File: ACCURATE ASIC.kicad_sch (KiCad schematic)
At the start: 51 parts, among them IC1 CERN_aCCURATE2_A_Chip1, IC2 AD817ARZ, IC3 DAC7578SRGE, IC4 AD817ARZ, IC5 AD817ARZ, IC6 ADR443BRZ, IC7 NL17SV16XV5T2G, U1 SHT4x

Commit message: Begun schematics
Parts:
- removed C11, C26, C28: CC0603_100NF_50V_10%_X7R, Capacitors SMD:CAPC1608X87N, symbol Capacitors SMD:CC0603_100NF_50V_10%_X7R
- removed C27: CC0603_10UF_25V_20%_X5R, Capacitors SMD:CAPC1709X100N, symbol Capacitors SMD:CC0603_10UF_25V_20%_X5R
- removed IC6: ADR443BRZ, ICs And Semiconductors SMD:SOIC127P600X175-8N, symbol Regulators:ADR443BRZ
- removed IC7: NL17SV16XV5T2G, ICs And Semiconductors SMD:SOTFL50P160X60-5N, symbol Standard Logic:NL17SV16XV5T2G
- removed R14, R15: R0603_0R_JUMPER, Resistors SMD:RESC1608X55N, symbol Resistors SMD:R0603_0R_JUMPER
- removed R2, R3: R0805_10K_0.1%_0.1W_10PPM, Resistors SMD:RESC2012X60N, symbol Resistors SMD:R0805_10K_0.1%_0.1W_10PPM
- removed U1: SHT4x, Sensor_Humidity:Sensirion_DFN-4_1.5x1.5mm_P0.8mm_SHT4x_NoCentralPad, symbol Sensor_Humidity:SHT4x
- added C67, C69: CC0603_100NF_50V_10%_X7R, Capacitors SMD:CAPC1608X87N, symbol Capacitors SMD:CC0603_100NF_50V_10%_X7R
- added C68: CC0603_220NF_10V_10%_X7R, Capacitors SMD:CAPC1608X87N, symbol Capacitors SMD:CC0603_220NF_10V_10%_X7R
- added C70: CC0603_10UF_25V_20%_X5R, Capacitors SMD:CAPC1709X100N, symbol Capacitors SMD:CC0603_10UF_25V_20%_X5R
- added J8: Conn_02x04_Counter_Clockwise, symbol Connector_Generic:Conn_02x04_Counter_Clockwise
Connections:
- net GND: now also C69.2, C70.2
- net SCL: now also J8.5 (Pin_5), J8.7 (Pin_7)
- net SDA: now also J8.6 (Pin_6), J8.8 (Pin_8)
- net Vcm_Buf: now also C67.1, C68.1, C69.1, C70.1
- net at IC1.2, TP1.1: now also C67.2, C68.2
- net +5VA renamed +5V
- net 3V3_Ref renamed 3V_Ref
- new net FPGA_SCL: J8.2 (Pin_2)
- new net FPGA_SDA: J8.1 (Pin_1)
- new net MCU_SCL: J8.4 (Pin_4)
- new net MCU_SDA: J8.3 (Pin_3)
- no-connect marks 20 -> 17
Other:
- note added: ": :||"
- note added: "||: :"
- note removed: "3V3 Reference"
- note removed: "ACCURATE2 Clock Generation"
- note removed: "Humidity and Temperature sensor"
- moved on the sheet: C1, C2, C3, C4, C5, C6, C7, C8, IC1, R1, TP1

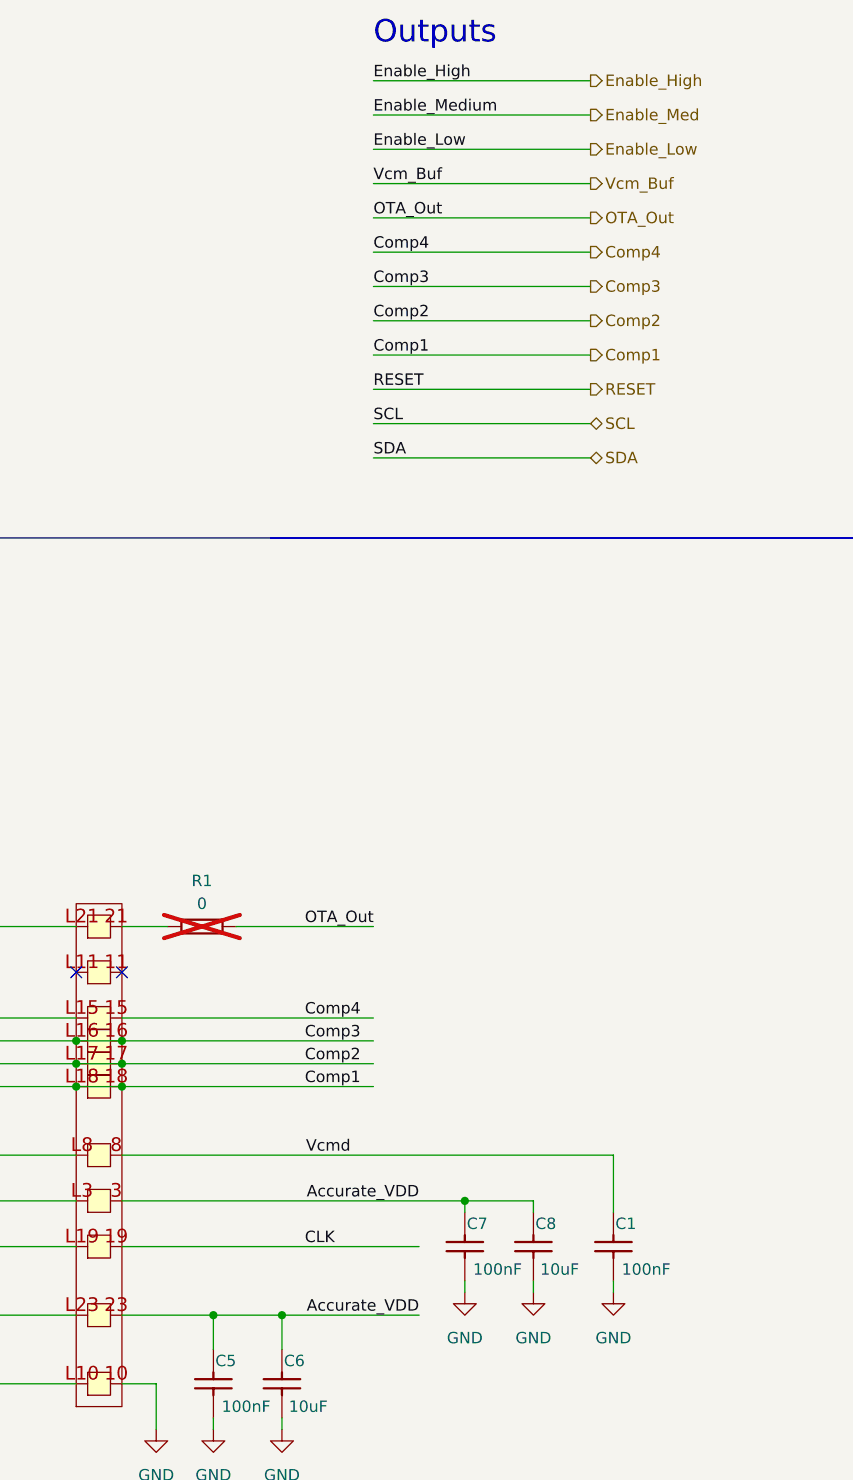
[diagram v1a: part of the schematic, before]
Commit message: Connected FPGA to Accurate, added Atsam, fixed some Accurate connections
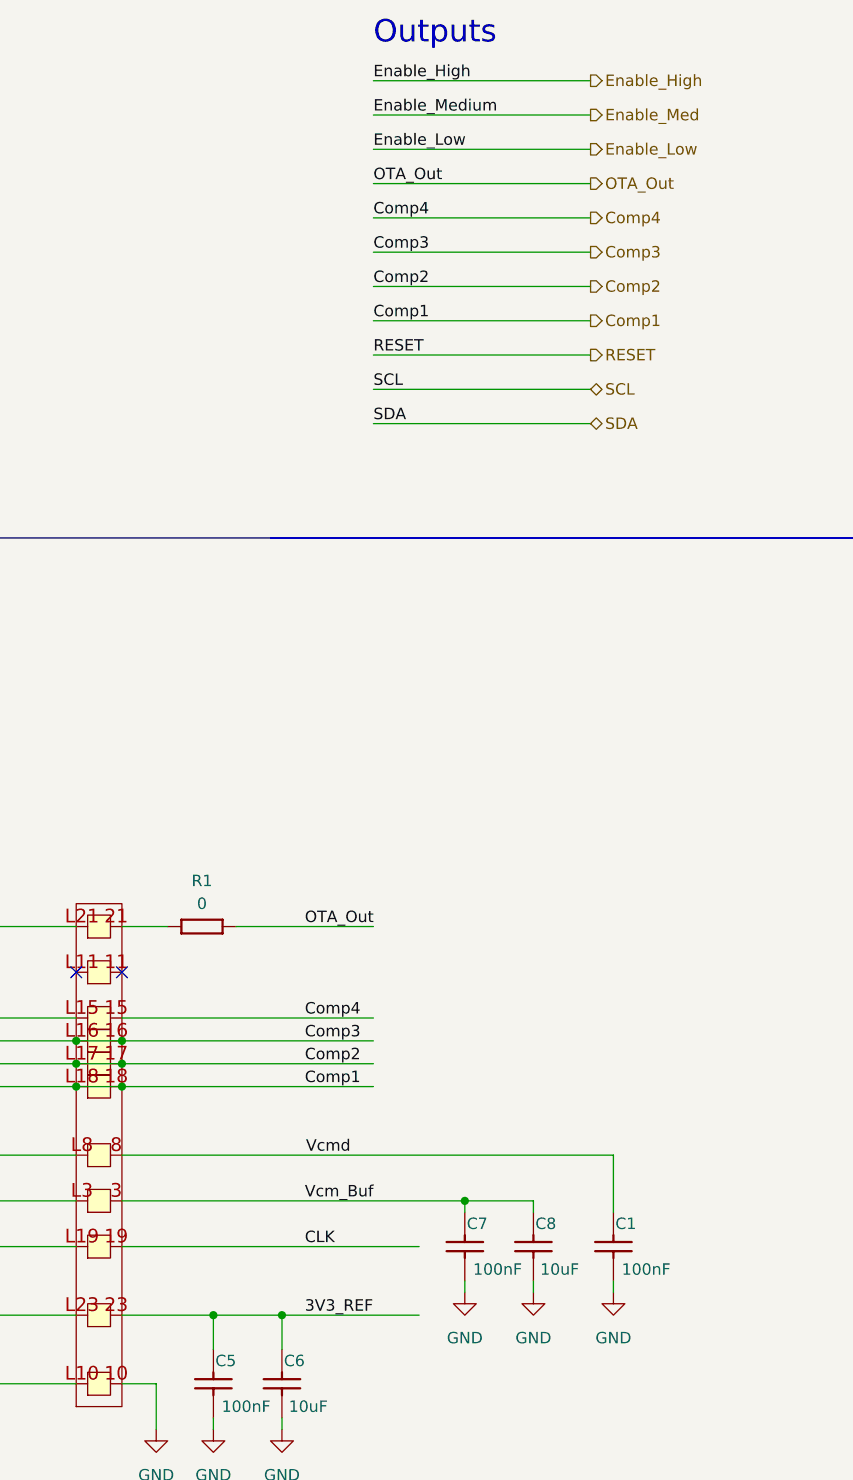
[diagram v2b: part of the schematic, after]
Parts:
- R1: now fitted
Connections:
- net 3V3_REF: now also C5.1, C6.1, IC1.23
- net Vcm_Buf: now also C7.1, C8.1, IC1.3
- removed net Accurate_VDD: C5.1, C6.1, C7.1, C8.1, IC1.23, IC1.3
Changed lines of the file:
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@@
     (stroke (width 0) (type default))
   )
-  (wire (pts (xy 339.09 43.18) (xy 363.22 43.18))
+  (wire (pts (xy 339.09 39.37) (xy 363.22 39.37))
     (stroke (width 0) (type default))
   )
@@
     (stroke (width 0) (type default))
   )
-  (wire (pts (xy 339.09 35.56) (xy 363.22 35.56))
-    (stroke (width 0) (type default))
-  )
   (wire (pts (xy 228.6 101.6) (xy 232.41 101.6))
     (stroke (width 0) (type default))
@@
     (stroke (width 0) (type default))
   )
-  (wire (pts (xy 311.15 148.59) (xy 349.25 148.59))
-    (stroke (width 0) (type default))
-  )
   (polyline (pts (xy 327.66 74.93) (xy 407.9748 74.93))
     (stroke (width 0) (type default))
@@
     (stroke (width 0) (type default))
   )
-  (wire (pts (xy 339.09 39.37) (xy 363.22 39.37))
+  (wire (pts (xy 339.09 35.56) (xy 363.22 35.56))
     (stroke (width 0) (type default))
   )
@@
     (stroke (width 0) (type default))
   )
-  (wire (pts (xy 339.09 58.42) (xy 363.22 58.42))
+  (wire (pts (xy 339.09 54.61) (xy 363.22 54.61))
     (stroke (width 0) (type default))
   )
@@
     (stroke (width 0) (type default))
   )
+  (wire (pts (xy 311.15 148.59) (xy 349.25 148.59))
+    (stroke (width 0) (type default))
+  )
   (wire (pts (xy 55.88 222.25) (xy 58.42 222.25))
     (stroke (width 0) (type default))
@@
     (stroke (width 0) (type default))
   )
-  (wire (pts (xy 339.09 54.61) (xy 363.22 54.61))
+  (wire (pts (xy 339.09 50.8) (xy 363.22 50.8))
     (stroke (width 0) (type default))
   )
@@
     (stroke (width 0) (type default))
   )
-  (wire (pts (xy 339.09 46.99) (xy 363.22 46.99))
+  (wire (pts (xy 339.09 43.18) (xy 363.22 43.18))
     (stroke (width 0) (type default))
   )
-  (wire (pts (xy 339.09 50.8) (xy 363.22 50.8))
+  (wire (pts (xy 339.09 46.99) (xy 363.22 46.99))
     (stroke (width 0) (type default))
   )
@@
     (stroke (width 0) (type default))
   )
-  (wire (pts (xy 339.09 62.23) (xy 363.22 62.23))
+  (wire (pts (xy 339.09 58.42) (xy 363.22 58.42))
     (stroke (width 0) (type default))
   )
@@
     (stroke (width 0) (type default))
   )
-  (wire (pts (xy 339.09 66.04) (xy 363.22 66.04))
+  (wire (pts (xy 339.09 62.23) (xy 363.22 62.23))
     (stroke (width 0) (type default))
   )
@@
     (effects (font (size 1.27 1.27)) (justify left bottom))
   )
-  (label "Comp3" (at 339.09 46.99 0) (fields_autoplaced)
+  (label "Comp3" (at 339.09 43.18 0) (fields_autoplaced)
     (effects (font (size 1.27 1.27)) (justify left bottom))
   )
@@
     (effects (font (size 1.27 1.27)) (justify right bottom))
   )
-  (label "Comp2" (at 339.09 50.8 0) (fields_autoplaced)
+  (label "Comp2" (at 339.09 46.99 0) (fields_autoplaced)
     (effects (font (size 1.27 1.27)) (justify left bottom))
   )
@@
     (effects (font (size 1.27 1.27)) (justify left bottom))
   )
-  (label "Comp1" (at 339.09 54.61 0) (fields_autoplaced)
+  (label "Comp1" (at 339.09 50.8 0) (fields_autoplaced)
     (effects (font (size 1.27 1.27)) (justify left bottom))
   )
@@
     (effects (font (size 1.27 1.27)) (justify left bottom))
   )
-  (label "Comp4" (at 339.09 43.18 0) (fields_autoplaced)
+  (label "Comp4" (at 339.09 39.37 0) (fields_autoplaced)
     (effects (font (size 1.27 1.27)) (justify left bottom))
   )
-  (label "Accurate_VDD" (at 344.17 161.29 180) (fields_autoplaced)
-    (effects (font (size 1.27 1.27)) (justify right bottom))
+  (label "Vcm_Buf" (at 331.47 148.59 0) (fields_autoplaced)
+    (effects (font (size 1.27 1.27)) (justify left bottom))
   )
   (label "3V_REF" (at 41.91 72.39 0) (fields_autoplaced)
@@
     (effects (font (size 1.27 1.27)) (justify left bottom))
   )
-  (label "SCL" (at 339.09 62.23 0) (fields_autoplaced)
+  (label "SCL" (at 339.09 58.42 0) (fields_autoplaced)
     (effects (font (size 1.27 1.27)) (justify left bottom))
   )
@@
     (effects (font (size 1.27 1.27)) (justify right bottom))
   )
+  (label "3V3_REF" (at 331.47 161.29 0) (fields_autoplaced)
+    (effects (font (size 1.27 1.27)) (justify left bottom))
+  )
   (label "Comp1" (at 331.47 135.89 0) (fields_autoplaced)
     (effects (font (size 1.27 1.27)) (justify left bottom))
@@
     (effects (font (size 1.27 1.27)) (justify left bottom))
   )
-  (label "SDA" (at 339.09 66.04 0) (fields_autoplaced)
+  (label "SDA" (at 339.09 62.23 0) (fields_autoplaced)
     (effects (font (size 1.27 1.27)) (justify left bottom))
   )
@@
     (effects (font (size 1.27 1.27)) (justify left bottom))
   )
-  (label "OTA_Out" (at 339.09 39.37 0) (fields_autoplaced)
+  (label "OTA_Out" (at 339.09 35.56 0) (fields_autoplaced)
     (effects (font (size 1.27 1.27)) (justify left bottom))
   )
@@
     (effects (font (size 1.27 1.27)) (justify left bottom))
   )
-  (label "Vcm_Buf" (at 339.09 35.56 0) (fields_autoplaced)
-    (effects (font (size 1.27 1.27)) (justify left bottom))
-  )
   (label "FPGA_SDA" (at 86.36 34.29 0) (fields_autoplaced)
     (effects (font (size 1.27 1.27)) (justify left bottom))
   )
-  (label "Accurate_VDD" (at 344.17 148.59 180) (fields_autoplaced)
-    (effects (font (size 1.27 1.27)) (justify right bottom))
-  )
   (label "Enable_Low" (at 226.06 156.21 0) (fields_autoplaced)
     (effects (font (size 1.27 1.27)) (justify left bottom))
   )
-  (label "RESET" (at 339.09 58.42 0) (fields_autoplaced)
+  (label "RESET" (at 339.09 54.61 0) (fields_autoplaced)
     (effects (font (size 1.27 1.27)) (justify left bottom))
   )
@@
     (effects (font (size 1.27 1.27)) (justify left bottom))
   )
-  (hierarchical_label "Comp2" (shape output) (at 363.22 50.8 0) (fields_autoplaced)
+  (hierarchical_label "Comp2" (shape output) (at 363.22 46.99 0) (fields_autoplaced)
     (effects (font (size 1.27 1.27)) (justify left))
   )
-  (hierarchical_label "SDA" (shape bidirectional) (at 363.22 66.04 0) (fields_autoplaced)
+  (hierarchical_label "SDA" (shape bidirectional) (at 363.22 62.23 0) (fields_autoplaced)
     (effects (font (size 1.27 1.27)) (justify left))
   )
-  (hierarchical_label "Comp1" (shape output) (at 363.22 54.61 0) (fields_autoplaced)
+  (hierarchical_label "Comp1" (shape output) (at 363.22 50.8 0) (fields_autoplaced)
     (effects (font (size 1.27 1.27)) (justify left))
   )
-  (hierarchical_label "RESET" (shape output) (at 363.22 58.42 0) (fields_autoplaced)
+  (hierarchical_label "RESET" (shape output) (at 363.22 54.61 0) (fields_autoplaced)
     (effects (font (size 1.27 1.27)) (justify left))
   )
@@
     (effects (font (size 1.27 1.27)) (justify left))
   )
-  (hierarchical_label "OTA_Out" (shape output) (at 363.22 39.37 0) (fields_autoplaced)
+  (hierarchical_label "OTA_Out" (shape output) (at 363.22 35.56 0) (fields_autoplaced)
     (effects (font (size 1.27 1.27)) (justify left))
   )
@@
     (effects (font (size 1.27 1.27)) (justify right))
   )
-  (hierarchical_label "Comp4" (shape output) (at 363.22 43.18 0) (fields_autoplaced)
+  (hierarchical_label "Comp4" (shape output) (at 363.22 39.37 0) (fields_autoplaced)
     (effects (font (size 1.27 1.27)) (justify left))
   )
@@
     (effects (font (size 1.27 1.27)) (justify right))
   )
-  (hierarchical_label "SCL" (shape bidirectional) (at 363.22 62.23 0) (fields_autoplaced)
+  (hierarchical_label "SCL" (shape bidirectional) (at 363.22 58.42 0) (fields_autoplaced)
     (effects (font (size 1.27 1.27)) (justify left))
   )
-  (hierarchical_label "Comp3" (shape output) (at 363.22 46.99 0) (fields_autoplaced)
-    (effects (font (size 1.27 1.27)) (justify left))
-  )
-  (hierarchical_label "Vcm_Buf" (shape output) (at 363.22 35.56 0) (fields_autoplaced)
+  (hierarchical_label "Comp3" (shape output) (at 363.22 43.18 0) (fields_autoplaced)
     (effects (font (size 1.27 1.27)) (justify left))
   )
@@
   )
   (symbol (lib_id "Resistors SMD:R0805_0R_JUMPER") (at 316.23 118.11 0) (unit 1)
-    (in_bom yes) (on_board yes) (dnp yes) (fields_autoplaced)
+    (in_bom yes) (on_board yes) (dnp no) (fields_autoplaced)
     (property "Reference" "R1" (at 320.04 113.03 0)
       (effects (font (size 1.27 1.27)))

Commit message: Made MCU schematic, made root schematic, adding ESD diodes, fixed  EDR errors
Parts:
- removed J8: Conn_02x04_Counter_Clockwise, symbol Connector_Generic:Conn_02x04_Counter_Clockwise
- added D1 (x4): SMBJ3V3, ICs And Semiconductors SMD:DIOM5436X244N, symbol Diodes:SMBJ3V3
- added D6: PESD3V3L5UY, Package_TO_SOT_SMD:SOT-363_SC-70-6, symbol Power_Protection:PESD3V3L5UY
- added J12: Conn_02x03_Counter_Clockwise, symbol Connector_Generic:Conn_02x03_Counter_Clockwise
- added J14: Conn_01x03, symbol Connector_Generic:Conn_01x03
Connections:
- net 3V_Ref is gone; now on net 3V_REF: IC3.8 (VREFIN)
- net CLK: now also D1.1 (C), J14.2 (Pin_2)
- net Comp1: no longer IC1.D18 (Comp1), IC1.L18
- net Comp2: no longer IC1.D17 (Comp2), IC1.L17
- net Comp3: no longer IC1.D16 (Comp3), IC1.L16
- net FPGA_SCL: now also D6.4 (K3), J12.1 (Pin_1)
- net FPGA_SDA: now also D1.1 (C), J12.6 (Pin_6)
- net GND: now also D1.2 (A), D1.2 (A), D1.2 (A), D1.2 (A), D6.2 (A)
- net MCU_SCL: now also D6.1 (K1), J12.3 (Pin_3)
- net MCU_SDA: now also D6.6 (K5), J12.4 (Pin_4)
- net SCL: now also D6.3 (K2), J12.2 (Pin_2)
- net SDA: now also D6.5 (K4), J12.5 (Pin_5)
- net Enable_High renamed Enable.High
- net Enable_Low renamed Enable.Low
- net Enable_Med renamed Enable.Medium
- new net: IC1.D16 (Comp3), IC1.L16
- new net: IC1.D17 (Comp2), IC1.L17
- new net: IC1.D18 (Comp1), IC1.L18
- new net EXT_CLK: D1.1 (C), J14.1 (Pin_1)
- new net FPGA_CLK: D1.1 (C), J14.3 (Pin_3)
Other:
- note added: "FPGA/External Clock Header"
- note added: "FPGA/MCU I2C Header"
- note added: "Power Ports"
- note added: "Shielding"
- note removed: ": :||"
- note removed: "||: :"
- moved on the sheet: C1, C10, C12, C13, C14, C15, C16, C17, C18, C19, C2, C20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
